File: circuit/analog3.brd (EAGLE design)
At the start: 56.2 x 50.8 mm, 71 parts, among them IC1 AD8603UJ, IC2 74HC4052D, IC3 AD8603UJ, IC4 AD8221R, IC5 AD8221R, IC6 LM258, IC7 LM258

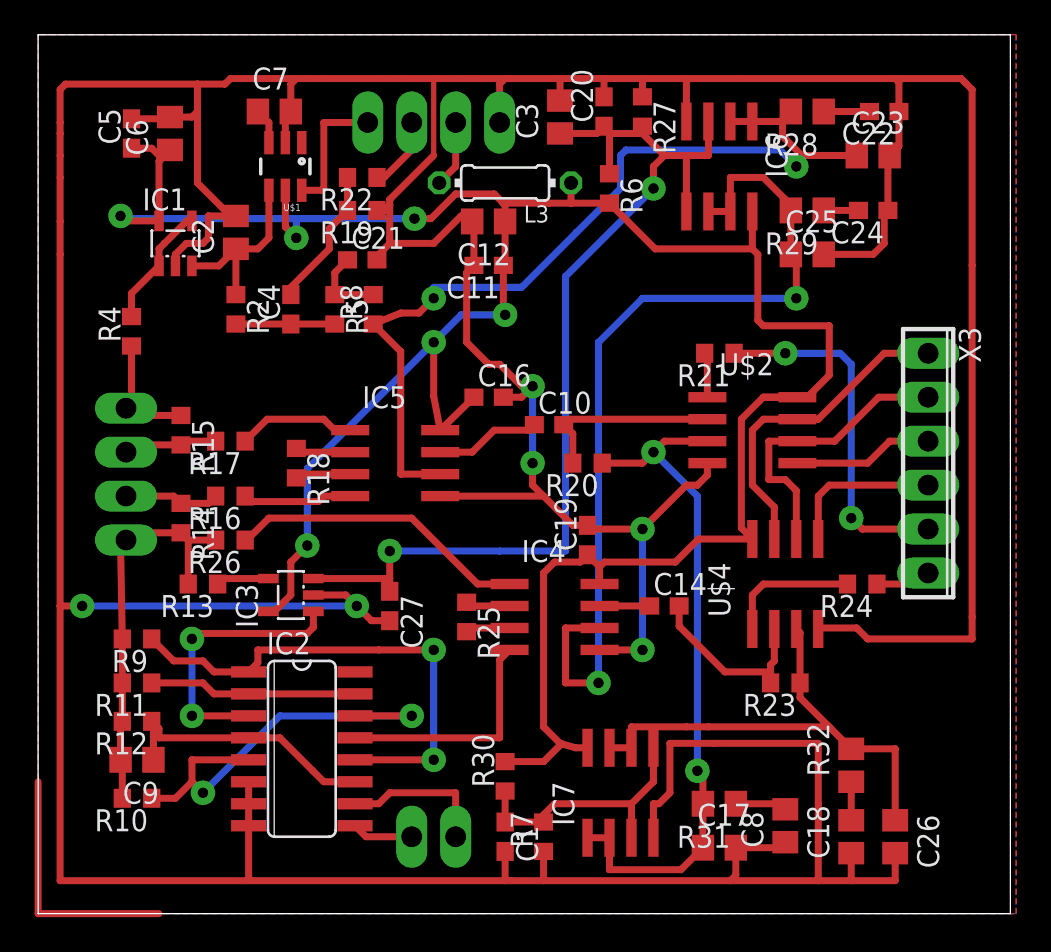
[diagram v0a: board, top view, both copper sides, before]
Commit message: - совместили северные контакты - добавили RC цепочки между первым и вторым каскадом усиления - добавили неподключеный коннектор, чтобы было на чем держаться дисплею
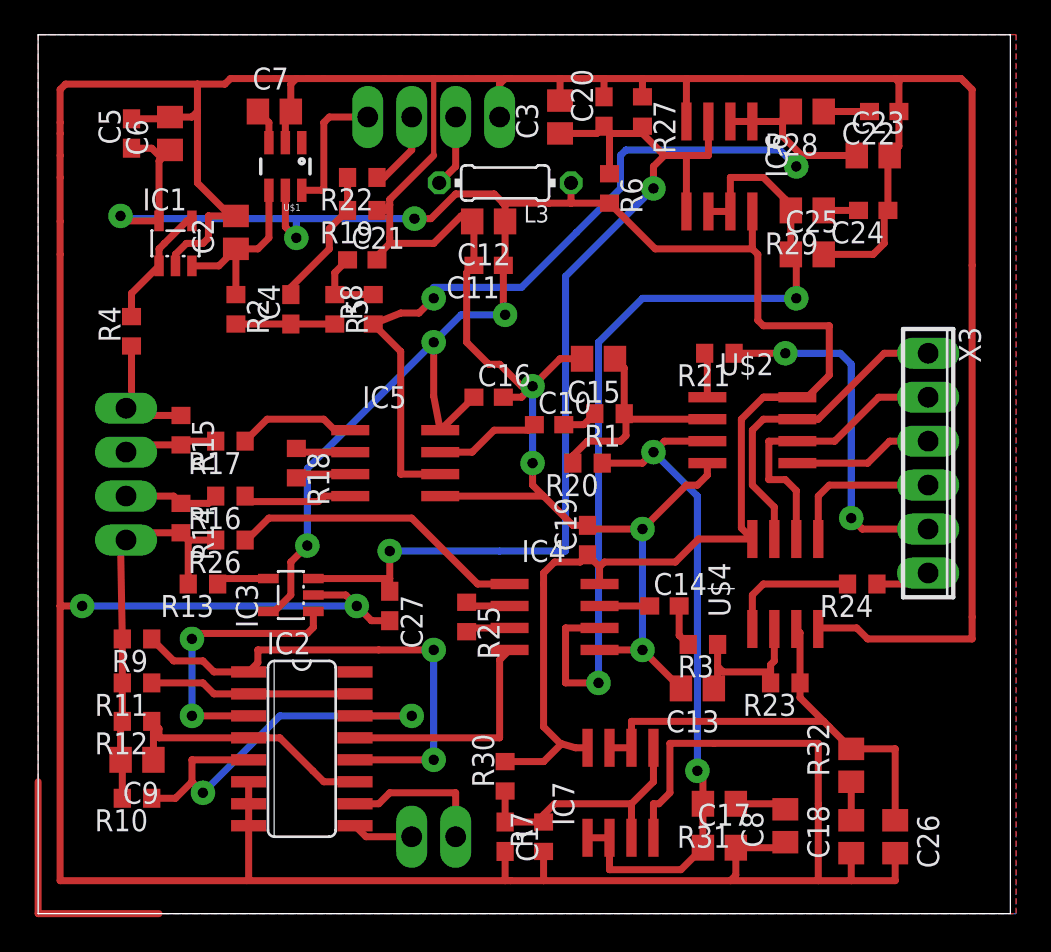
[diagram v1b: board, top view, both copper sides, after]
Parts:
- removed X2, X8: (no value), con-phoenix-254:2POL254
- added C13, C15: 330p, rcl:C0805
- added R1, R3: 1.2k, rcl:R0603
- added X5: (no value), con-phoenix-254:4POL254
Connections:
- new net N$37: C10.2, R1.2
- new net N$38: C14.2, R3.2
- net ANALOG_SW: now also X5.1; no longer X8.2
- net GENERATOR: now also X5.2; no longer X8.1
- net GNDA: now also C13.2, C15.2, X5.4; no longer X2.2
- net N$25: now also C13.1, R3.1; no longer C14.2
- net N$27: now also C15.1, R1.1; no longer C10.2
- net N$6: now also X5.3; no longer X2.1
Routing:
- net GNDA: track 362.1 -> 368.5 mm
- net N$27: track 10.9 -> 13.6 mm
- net N$38: track 0.00 -> 2.44 mm
- net N$37: track 0.00 -> 2.06 mm
- net N$25: track 10.8 -> 9.03 mm

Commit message: - переместили схемы чуть ниже, чтобы уместиться в 49 мм высоты
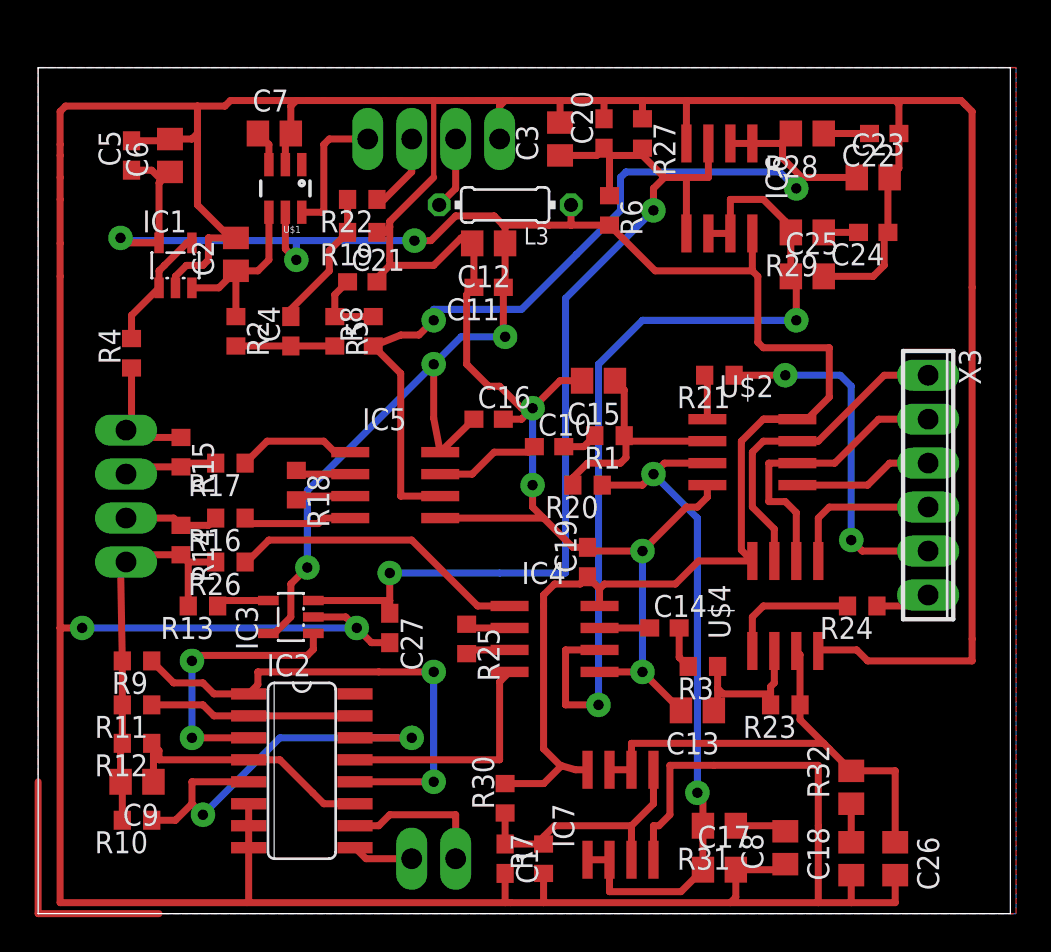
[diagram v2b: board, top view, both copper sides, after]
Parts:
- moved C11 1.27 mm to (26.0, 36.2)
- moved C12 1.27 mm to (26.0, 38.7)
- moved C15 1.27 mm to (32.4, 30.8)
- moved C24 1.27 mm to (48.3, 39.4)
- moved C25 1.27 mm to (44.5, 36.8)
- moved C3 1.27 mm to (30.2, 44.8)
- moved C5 1.27 mm to (5.40, 43.8)
- moved C6 1.27 mm to (7.62, 43.8)
- moved IC6 1.27 mm to (39.4, 41.9)
- moved R19 1.27 mm to (18.7, 39.4)
- moved R22 1.27 mm to (18.7, 41.3)
- moved R29 1.27 mm to (44.5, 39.4)
- moved R4 1.27 mm to (5.40, 32.4)
- moved U$1 1.27 mm to (14.3, 41.9)
- moved X5 1.27 mm to (22.9, 44.8)
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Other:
- board size 56.2 x 50.8 mm -> 56.2 x 48.9 mm

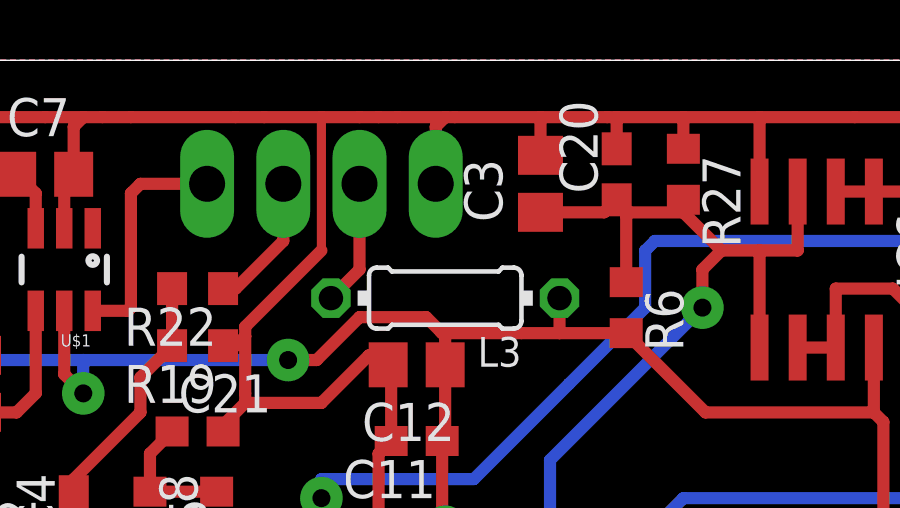
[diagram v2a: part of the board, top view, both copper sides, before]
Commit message: - поменяли местами питание и землю
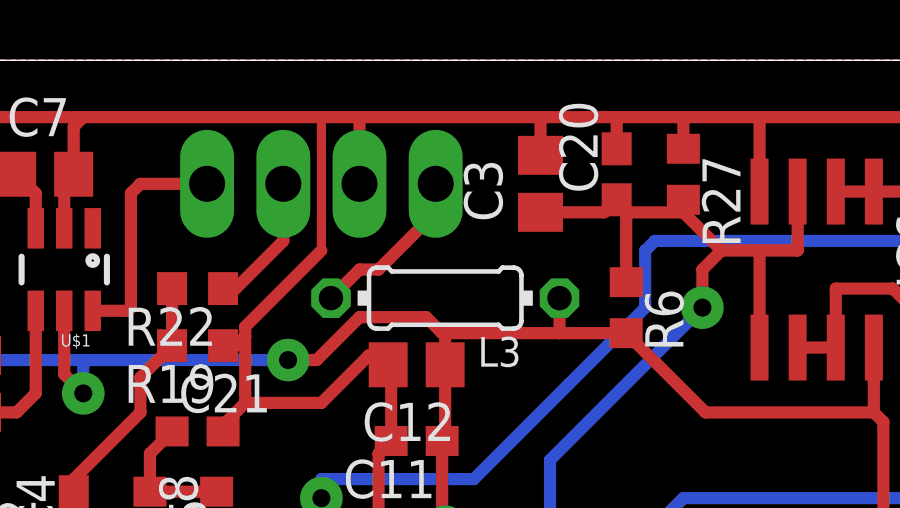
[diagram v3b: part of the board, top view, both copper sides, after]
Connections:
- net GNDA: now also X5.3; no longer X5.4
- net N$6: now also X5.4; no longer X5.3
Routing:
- net N$6: track 4.20 -> 5.63 mm
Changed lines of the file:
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@@
 <layer number="23" name="tOrigins" color="15" fill="1" visible="yes" active="yes"/>
 <layer number="24" name="bOrigins" color="15" fill="1" visible="yes" active="yes"/>
-<layer number="25" name="tNames" color="7" fill="1" visible="no" active="yes"/>
-<layer number="26" name="bNames" color="7" fill="1" visible="no" active="yes"/>
+<layer number="25" name="tNames" color="7" fill="1" visible="yes" active="yes"/>
+<layer number="26" name="bNames" color="7" fill="1" visible="yes" active="yes"/>
 <layer number="27" name="tValues" color="7" fill="1" visible="yes" active="yes"/>
 <layer number="28" name="bValues" color="7" fill="1" visible="yes" active="yes"/>
@@
 <wire x1="20.0025" y1="46.99" x2="16.51" y2="46.99" width="0.4064" layer="1"/>
 <wire x1="16.51" y1="46.99" x2="15.56" y2="46.99" width="0.4064" layer="1"/>
-<wire x1="27.305" y1="46.99" x2="26.9875" y2="46.99" width="0.4064" layer="1"/>
-<wire x1="26.9875" y1="46.99" x2="25.4" y2="46.99" width="0.4064" layer="1"/>
 <wire x1="25.4" y1="46.99" x2="24.765" y2="46.99" width="0.4064" layer="1"/>
 <wire x1="25.185" y1="36.195" x2="25.185" y2="38.635" width="0.4064" layer="1"/>
 <wire x1="25.185" y1="38.635" x2="25.085" y2="38.735" width="0.4064" layer="1"/>
 <wire x1="32.385" y1="46.99" x2="30.1625" y2="46.99" width="0.4064" layer="1"/>
-<wire x1="30.1625" y1="46.99" x2="27.305" y2="46.99" width="0.4064" layer="1"/>
 <wire x1="40.64" y1="46.99" x2="37.465" y2="46.99" width="0.4064" layer="1"/>
 <wire x1="37.465" y1="46.99" x2="34.925" y2="46.99" width="0.4064" layer="1"/>
@@
 <contactref element="U$1" pad="2"/>
 <contactref element="C7" pad="2"/>
-<wire x1="26.67" y1="46.6725" x2="26.9875" y2="46.99" width="0.4064" layer="1"/>
 <wire x1="38.1" y1="23.495" x2="37.465" y2="23.495" width="0.4064" layer="1"/>
 <wire x1="37.465" y1="23.495" x2="34.925" y2="20.955" width="0.4064" layer="1"/>
@@
 <wire x1="37.15" y1="11.7475" x2="37.1475" y2="11.7475" width="0.4064" layer="1"/>
 <wire x1="37.1475" y1="11.7475" x2="34.925" y2="13.97" width="0.4064" layer="1"/>
-<contactref element="X5" pad="4"/>
-<wire x1="26.67" y1="44.7675" x2="26.67" y2="46.6725" width="0.4064" layer="1"/>
-<wire x1="12.065" y1="0.635" x2="12.1666" y2="0.7366" width="0" layer="19" extent="1-1"/>
+<contactref element="X5" pad="3"/>
+<wire x1="24.13" y1="44.7675" x2="24.13" y2="46.99" width="0.4064" layer="1"/>
+<wire x1="25.4" y1="46.99" x2="30.1625" y2="46.99" width="0.4064" layer="1"/>
 </signal>
 <signal name="VCC">
@@
 </signal>
 <signal name="N$6">
+<contactref element="X5" pad="4"/>
 <contactref element="L3" pad="2"/>
-<contactref element="X5" pad="3"/>
-<wire x1="24.13" y1="44.7675" x2="24.13" y2="41.91" width="0.4064" layer="1"/>
+<wire x1="26.67" y1="44.7675" x2="26.67" y2="43.815" width="0.4064" layer="1"/>
+<wire x1="26.67" y1="43.815" x2="24.765" y2="41.91" width="0.4064" layer="1"/>
+<wire x1="24.765" y1="41.91" x2="24.13" y2="41.91" width="0.4064" layer="1"/>
 <wire x1="24.13" y1="41.91" x2="23.1775" y2="40.9575" width="0.4064" layer="1"/>
 </signal>

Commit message: - допаяли схему. - PC6 USB_ON подключили - PB10 AN_SW подключили
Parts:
- IC1, IC3: value AD8603UJ -> AD8605
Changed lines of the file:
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@@
 <layers>
 <layer number="1" name="Top" color="4" fill="1" visible="yes" active="yes"/>
-<layer number="16" name="Bottom" color="1" fill="1" visible="yes" active="yes"/>
+<layer number="16" name="Bottom" color="1" fill="1" visible="no" active="yes"/>
 <layer number="17" name="Pads" color="2" fill="1" visible="yes" active="yes"/>
 <layer number="18" name="Vias" color="2" fill="1" visible="yes" active="yes"/>
@@
 <layer number="23" name="tOrigins" color="15" fill="1" visible="yes" active="yes"/>
 <layer number="24" name="bOrigins" color="15" fill="1" visible="yes" active="yes"/>
-<layer number="25" name="tNames" color="7" fill="1" visible="yes" active="yes"/>
-<layer number="26" name="bNames" color="7" fill="1" visible="yes" active="yes"/>
-<layer number="27" name="tValues" color="7" fill="1" visible="yes" active="yes"/>
-<layer number="28" name="bValues" color="7" fill="1" visible="yes" active="yes"/>
+<layer number="25" name="tNames" color="7" fill="1" visible="no" active="yes"/>
+<layer number="26" name="bNames" color="7" fill="1" visible="no" active="yes"/>
+<layer number="27" name="tValues" color="7" fill="1" visible="no" active="yes"/>
+<layer number="28" name="bValues" color="7" fill="1" visible="no" active="yes"/>
 <layer number="29" name="tStop" color="7" fill="3" visible="yes" active="yes"/>
 <layer number="30" name="bStop" color="7" fill="6" visible="yes" active="yes"/>
@@
 <element name="C25" library="rcl" package="C0805" value="47n" x="44.45" y="36.83"/>
 <element name="R29" library="rcl" package="R0805" value="5" x="44.45" y="39.37" rot="R180"/>
-<element name="IC3" library="analog-devices" package="SOT23-5" value="AD8603UJ" x="14.605" y="17.145" rot="R90">
+<element name="IC3" library="analog-devices" package="SOT23-5" value="AD8605" x="14.605" y="17.145" rot="R90">
 <attribute name="OC_NEWARK" value="59K6904" x="14.605" y="17.145" size="1.778" layer="27" rot="R90" display="off"/>
 <attribute name="MPN" value="AD8603AUJZ-REEL7" x="14.605" y="17.145" size="1.778" layer="27" rot="R90" display="off"/>
@@
 <element name="C26" library="rcl" package="C0805" value="47n" x="49.53" y="3.175" rot="R270"/>
 <element name="C27" library="rcl" package="C0603" value="100n" x="20.32" y="16.51" rot="R270"/>
-<element name="IC1" library="analog-devices" package="SOT23-5" value="AD8603UJ" x="7.9375" y="37.465">
+<element name="IC1" library="analog-devices" package="SOT23-5" value="AD8605" x="7.9375" y="37.465">
 <attribute name="OC_NEWARK" value="59K6904" x="7.9375" y="37.465" size="1.778" layer="27" display="off"/>
 <attribute name="MPN" value="AD8603AUJZ-REEL7" x="7.9375" y="37.465" size="1.778" layer="27" display="off"/>

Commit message: - обновили значения элементов
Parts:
- R21, R24: value 1.2k -> 120
- R30: value 56k -> 47k
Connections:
- net +2.2V1 renamed +2.5V3
- net +2.2V2 renamed +2.5V4
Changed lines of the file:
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@@
 <element name="C11" library="rcl" package="C0603" value="100n" x="26.035" y="36.195" rot="R180"/>
 <element name="C12" library="rcl" package="C0805" value="10mk" x="26.035" y="38.735" rot="R180"/>
-<element name="R21" library="rcl" package="R0603" value="1.2k" x="39.37" y="31.115" rot="R180"/>
+<element name="R21" library="rcl" package="R0603" value="120" x="39.37" y="31.115" rot="R180"/>
 <element name="U$4" library="balmer" package="SO8" value="MCP6S21" x="43.18" y="17.78"/>
 <element name="C14" library="rcl" package="C0603" value="1mk" x="36.195" y="16.51"/>
 <element name="R23" library="rcl" package="R0603" value="56k" x="43.18" y="12.065" rot="R180"/>
-<element name="R24" library="rcl" package="R0603" value="1.2k" x="47.625" y="17.78" rot="R180"/>
+<element name="R24" library="rcl" package="R0603" value="120" x="47.625" y="17.78" rot="R180"/>
 <element name="R25" library="rcl" package="R0603" value="18k" x="24.765" y="15.875" rot="R270"/>
 <element name="R26" library="rcl" package="R0603" value="1k" x="11.1125" y="20.32" rot="R180"/>
@@
 <element name="IC7" library="linear" package="SO08" value="LM258" x="33.655" y="5.715"/>
 <element name="R7" library="rcl" package="R0603" value="47k" x="29.21" y="3.175" rot="R90"/>
-<element name="R30" library="rcl" package="R0603" value="56k" x="26.9875" y="6.6675" rot="R90"/>
+<element name="R30" library="rcl" package="R0603" value="47k" x="26.9875" y="6.6675" rot="R90"/>
 <element name="R31" library="rcl" package="R0805" value="22" x="39.37" y="5.08" rot="R180"/>
 <element name="C8" library="rcl" package="C0805" value="10mk" x="43.18" y="3.81" rot="R90"/>
@@
 <wire x1="46.99" y1="4.125" x2="46.99" y2="6.3525" width="0.4064" layer="1"/>
 </signal>
-<signal name="+2.2V1">
+<signal name="+2.5V3">
 <contactref element="IC7" pad="1"/>
 <contactref element="R31" pad="2"/>
@@
 <wire x1="38.42" y1="2.54" x2="38.42" y2="5.08" width="0.4064" layer="1"/>
 </signal>
-<signal name="+2.2V2">
+<signal name="+2.5V4">
 <contactref element="IC7" pad="6"/>
 <contactref element="IC7" pad="7"/>
